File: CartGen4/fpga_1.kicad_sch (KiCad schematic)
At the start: 5 parts, among them U9 LFXP2-8E-5MN132C

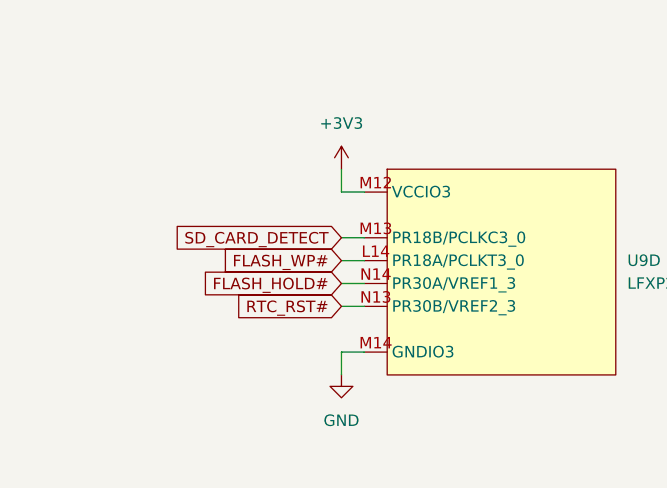
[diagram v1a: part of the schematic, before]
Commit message: Wired general purpose signals
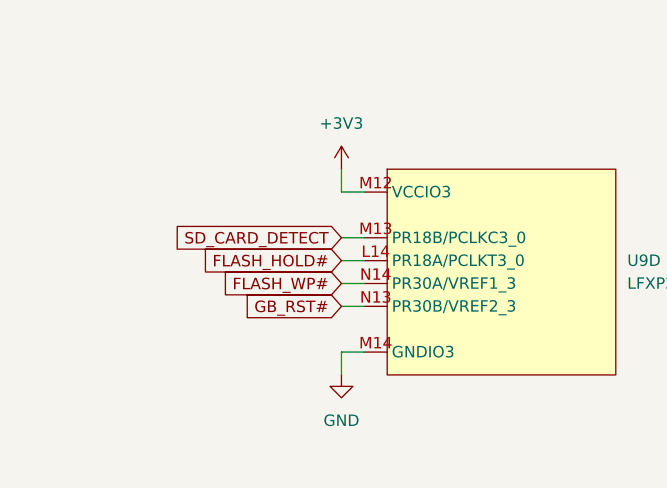
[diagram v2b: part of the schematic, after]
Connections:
- net FLASH_HOLD#: now also U9.L14 (PR18A/PCLKT3_0); no longer U9.N14 (PR30A/VREF1_3)
- net FLASH_WP#: now also U9.N14 (PR30A/VREF1_3); no longer U9.L14 (PR18A/PCLKT3_0)
- net RTC_RST# renamed GB_RST#
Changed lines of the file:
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@@
     )
   )
-  (global_label "FLASH_WP#" (shape input) (at 50.8 151.13 180) (fields_autoplaced)
+  (global_label "FLASH_HOLD#" (shape input) (at 50.8 151.13 180) (fields_autoplaced)
     (effects (font (size 1.27 1.27)) (justify right))
-    (property "Intersheet References" "${INTERSHEET_REFS}" (id 0) (at 37.6826 151.0506 0)
+    (property "Intersheet References" "${INTERSHEET_REFS}" (id 0) (at 35.445 151.0506 0)
       (effects (font (size 1.27 1.27)) (justify right) hide)
     )
@@
     )
   )
+  (global_label "GB_RST#" (shape input) (at 50.8 156.21 180) (fields_autoplaced)
+    (effects (font (size 1.27 1.27)) (justify right))
+    (property "Intersheet References" "${INTERSHEET_REFS}" (id 0) (at 40.1621 156.2894 0)
+      (effects (font (size 1.27 1.27)) (justify right) hide)
+    )
+  )
   (global_label "GB_ADDR[0..15]" (shape input) (at 115.57 39.37 180) (fields_autoplaced)
     (effects (font (size 1.27 1.27)) (justify right))
@@
     )
   )
-  (global_label "RTC_RST#" (shape input) (at 50.8 156.21 180) (fields_autoplaced)
+  (global_label "FLASH_WP#" (shape input) (at 50.8 153.67 180) (fields_autoplaced)
     (effects (font (size 1.27 1.27)) (justify right))
-    (property "Intersheet References" "${INTERSHEET_REFS}" (id 0) (at 39.1945 156.1306 0)
+    (property "Intersheet References" "${INTERSHEET_REFS}" (id 0) (at 37.6826 153.5906 0)
       (effects (font (size 1.27 1.27)) (justify right) hide)
     )
@@
       (effects (font (size 1.27 1.27)) (justify right) hide)
     )
-  )
-  (global_label "FLASH_HOLD#" (shape input) (at 50.8 153.67 180) (fields_autoplaced)
-    (effects (font (size 1.27 1.27)) (justify right))
-    (property "Intersheet References" "${INTERSHEET_REFS}" (id 0) (at 35.445 153.5906 0)
-      (effects (font (size 1.27 1.27)) (justify right) hide)
-    )

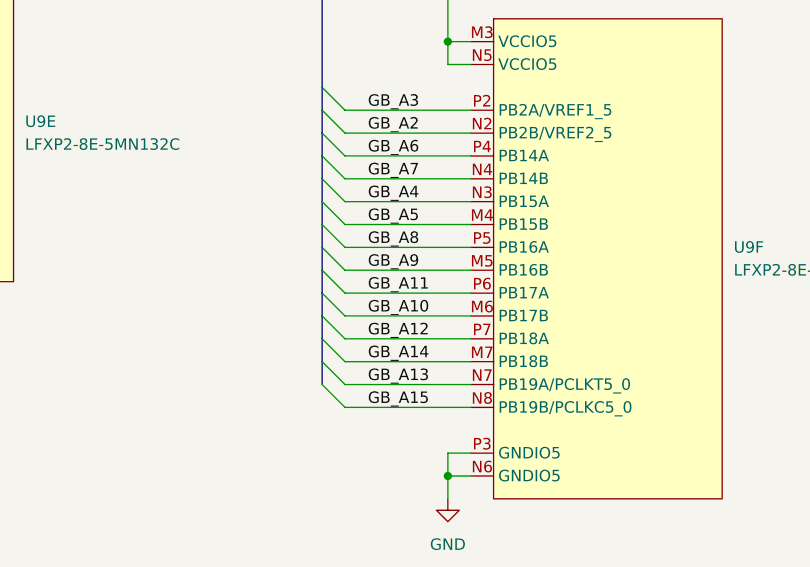
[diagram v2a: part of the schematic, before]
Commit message: Wired 1V2 and 1V8 around FPGA and RAM
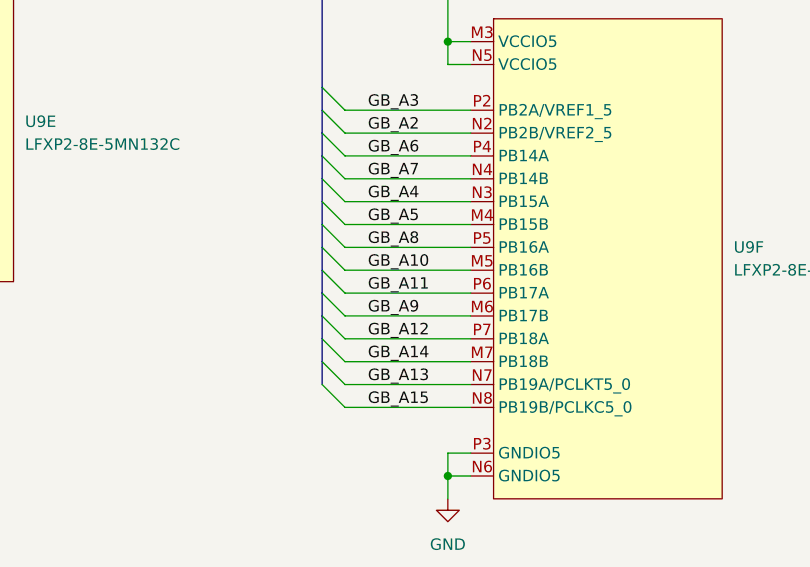
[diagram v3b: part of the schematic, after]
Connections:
- net GB_A10: now also U9.M5 (PB16B); no longer U9.M6 (PB17B)
- net GB_A9: now also U9.M6 (PB17B); no longer U9.M5 (PB16B)
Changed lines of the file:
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@@
     (effects (font (size 1.27 1.27)) (justify left bottom))
   )
-  (label "GB_A9" (at 130.81 85.09 0)
+  (label "GB_A9" (at 130.81 90.17 0)
     (effects (font (size 1.27 1.27)) (justify left bottom))
   )
@@
     (effects (font (size 1.27 1.27)) (justify left bottom))
   )
-  (label "GB_A10" (at 130.81 90.17 0)
-    (effects (font (size 1.27 1.27)) (justify left bottom))
-  )
   (label "GB_A4" (at 130.81 77.47 0)
     (effects (font (size 1.27 1.27)) (justify left bottom))
@@
     (effects (font (size 1.27 1.27)) (justify left bottom))
   )
+  (label "GB_A10" (at 130.81 85.09 0)
+    (effects (font (size 1.27 1.27)) (justify left bottom))
+  )

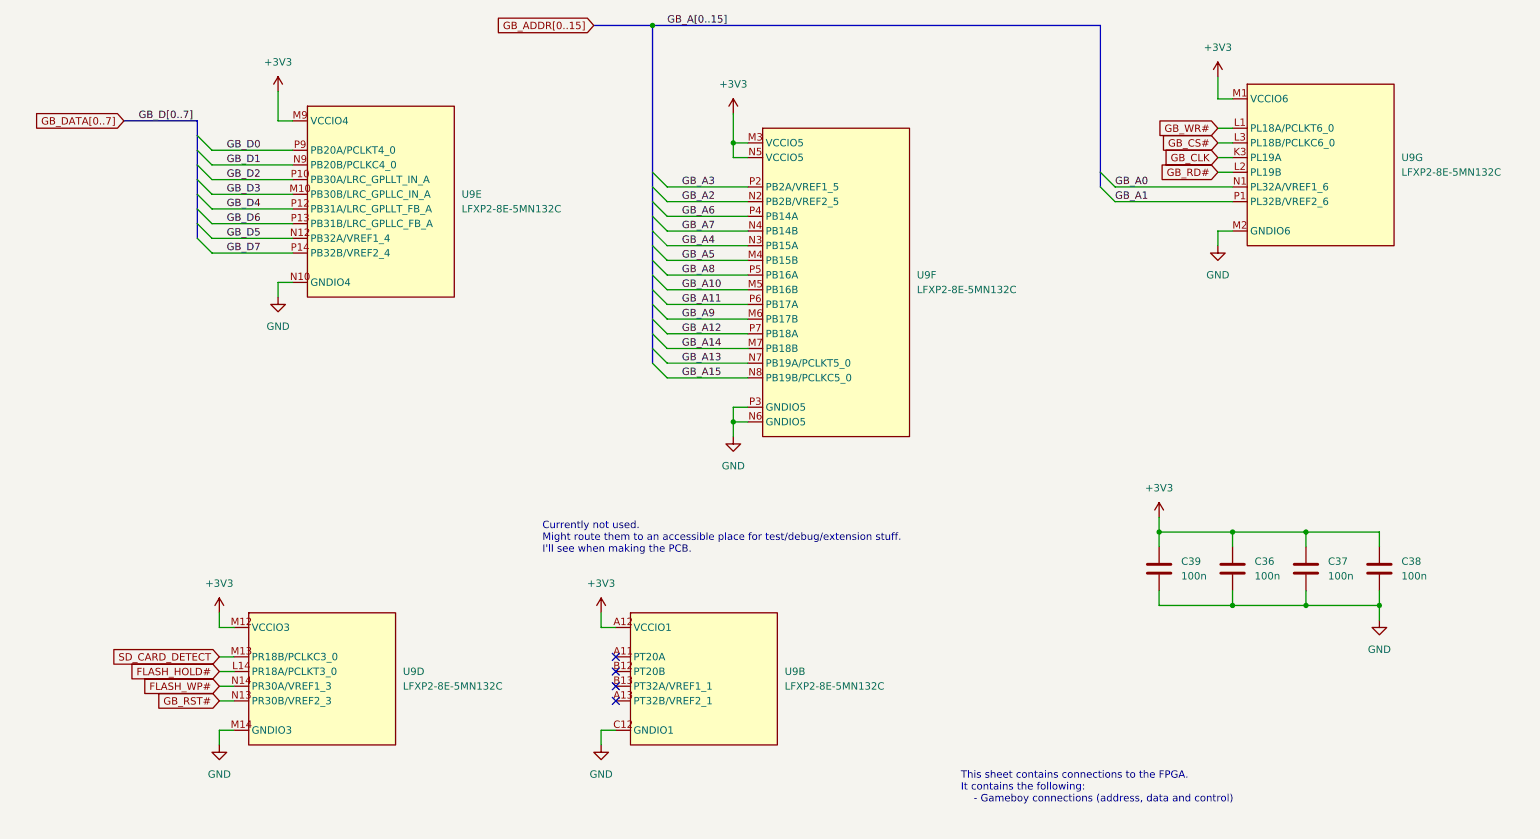
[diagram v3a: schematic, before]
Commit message: Rerouted some RAM and GB CTRL traces
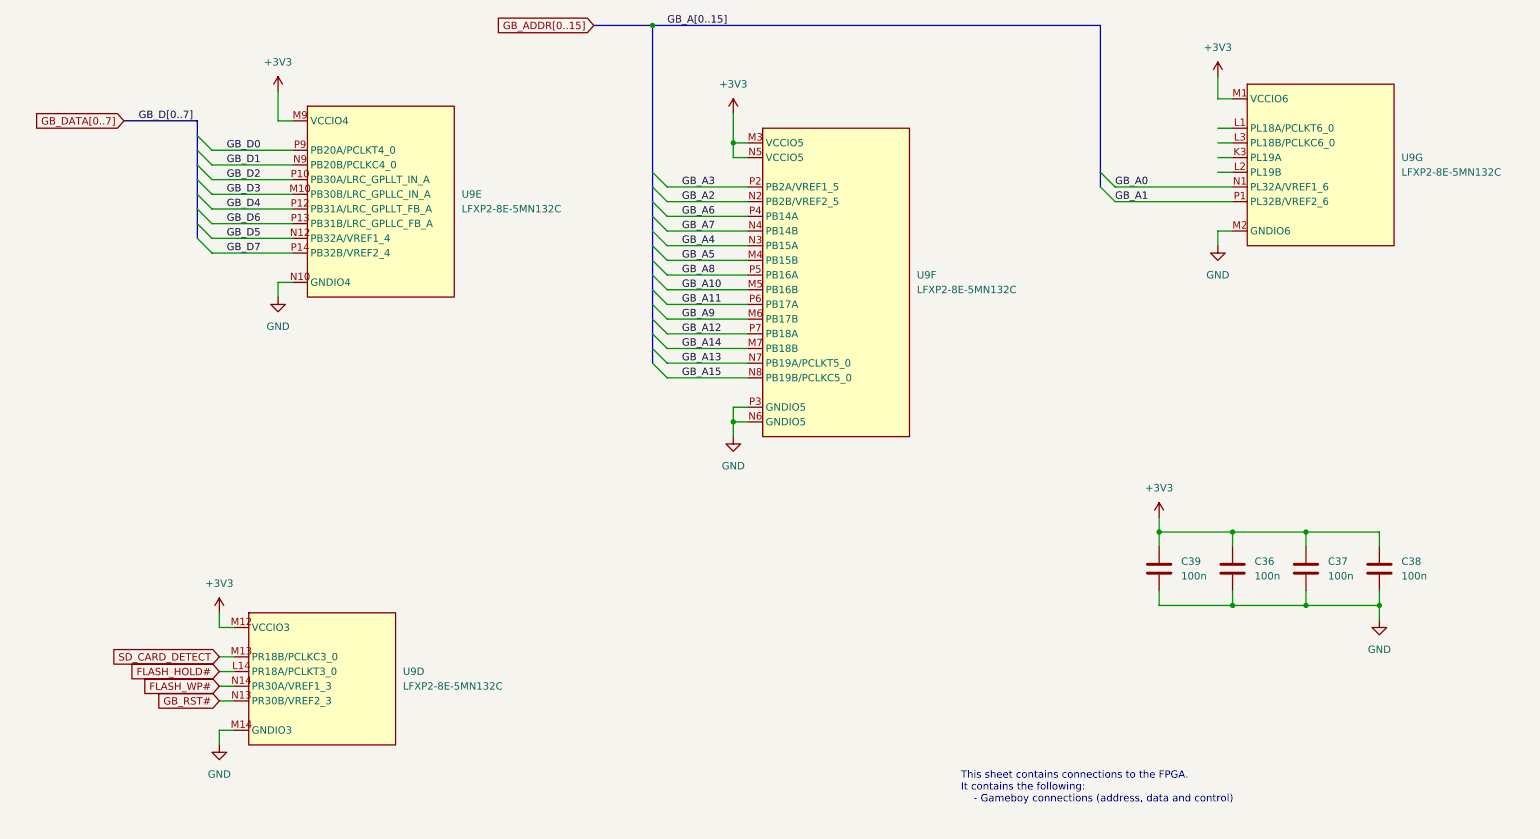
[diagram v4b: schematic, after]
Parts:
- removed unit 2 of U9
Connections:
- net GB_CLK: no longer names the net of U9.K3 (PL19A)
- net GB_CS#: no longer names the net of U9.L3 (PL18B/PCLKC6_0)
- net GB_RD#: no longer names the net of U9.L2 (PL19B)
- net GB_WR#: no longer names the net of U9.L1 (PL18A/PCLKT6_0)
- no-connect marks 4 -> 0
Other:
- note removed: "Currently not used. Might route them to an accessible place for test/debug/extension stuff. I'll see when making the PCB."
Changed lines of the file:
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@@
   (junction (at 139.7 59.69) (diameter 0) (color 0 0 0 0)
   )
-  (no_connect (at 119.38 156.21))
-  (no_connect (at 119.38 153.67))
-  (no_connect (at 119.38 151.13))
-  (no_connect (at 119.38 148.59))
   (bus_entry (at 46.99 73.66) (size 2.54 2.54)
     (stroke (width 0) (type default) (color 0 0 0 0))
@@
     (stroke (width 0) (type default) (color 0 0 0 0))
   )
-  (wire (pts (xy 116.84 143.51) (xy 116.84 140.97))
-    (stroke (width 0) (type default) (color 0 0 0 0))
-  )
-  (wire (pts (xy 119.38 161.29) (xy 116.84 161.29))
-    (stroke (width 0) (type default) (color 0 0 0 0))
-  )
   (wire (pts (xy 49.53 63.5) (xy 63.5 63.5))
     (stroke (width 0) (type default) (color 0 0 0 0))
@@
     (stroke (width 0) (type default) (color 0 0 0 0))
   )
-  (wire (pts (xy 116.84 161.29) (xy 116.84 163.83))
-    (stroke (width 0) (type default) (color 0 0 0 0))
-  )
   (wire (pts (xy 238.76 139.7) (xy 251.46 139.7))
     (stroke (width 0) (type default) (color 0 0 0 0))
@@
   )
   (wire (pts (xy 142.24 105.41) (xy 139.7 105.41))
-    (stroke (width 0) (type default) (color 0 0 0 0))
-  )
-  (wire (pts (xy 119.38 143.51) (xy 116.84 143.51))
     (stroke (width 0) (type default) (color 0 0 0 0))
   )
@@
     (effects (font (size 1.27 1.27)) (justify left bottom))
   )
-  (text "Currently not used.\nMight route them to an accessible place for test/debug/extension stuff.\nI'll see when making the PCB."
-    (at 106.68 130.81 0)
-    (effects (font (size 1.27 1.27)) (justify left bottom))
-  )
   (label "GB_D5" (at 52.07 76.2 0)
     (effects (font (size 1.27 1.27)) (justify left bottom))
@@
   (label "GB_A5" (at 130.81 80.01 0)
     (effects (font (size 1.27 1.27)) (justify left bottom))
-  )
-  (global_label "GB_CS#" (shape input) (at 223.52 59.69 180) (fields_autoplaced)
-    (effects (font (size 1.27 1.27)) (justify right))
-    (property "Intersheet References" "${INTERSHEET_REFS}" (id 0) (at 213.8498 59.6106 0)
-      (effects (font (size 1.27 1.27)) (justify right) hide)
-    )
   )
   (global_label "FLASH_HOLD#" (shape input) (at 50.8 151.13 180) (fields_autoplaced)
@@
     )
   )
-  (global_label "GB_RD#" (shape input) (at 223.52 64.77 180) (fields_autoplaced)
-    (effects (font (size 1.27 1.27)) (justify right))
-    (property "Intersheet References" "${INTERSHEET_REFS}" (id 0) (at 213.7893 64.6906 0)
-      (effects (font (size 1.27 1.27)) (justify right) hide)
-    )
-  )
   (global_label "SD_CARD_DETECT" (shape input) (at 50.8 148.59 180) (fields_autoplaced)
     (effects (font (size 1.27 1.27)) (justify right))
     (property "Intersheet References" "${INTERSHEET_REFS}" (id 0) (at 32.3002 148.6694 0)
-      (effects (font (size 1.27 1.27)) (justify right) hide)
-    )
-  )
-  (global_label "GB_CLK" (shape input) (at 223.52 62.23 180) (fields_autoplaced)
-    (effects (font (size 1.27 1.27)) (justify right))
-    (property "Intersheet References" "${INTERSHEET_REFS}" (id 0) (at 214.0312 62.1506 0)
-      (effects (font (size 1.27 1.27)) (justify right) hide)
-    )
-  )
-  (global_label "GB_WR#" (shape input) (at 223.52 57.15 180) (fields_autoplaced)
-    (effects (font (size 1.27 1.27)) (justify right))
-    (property "Intersheet References" "${INTERSHEET_REFS}" (id 0) (at 213.6079 57.0706 0)
       (effects (font (size 1.27 1.27)) (justify right) hide)
     )
@@
     (pin "1")
   )
-  (symbol (lib_id "power:+3V3") (at 116.84 140.97 0) (unit 1)
-    (in_bom yes) (on_board yes) (fields_autoplaced)
-    (property "Reference" "#PWR090" (id 0) (at 116.84 144.78 0)
-      (effects (font (size 1.27 1.27)) hide)
-    )
-    (property "Value" "+3V3" (id 1) (at 116.84 135.89 0))
-    (property "Footprint" "" (id 2) (at 116.84 140.97 0)
-      (effects (font (size 1.27 1.27)) hide)
-    )
-    (property "Datasheet" "" (id 3) (at 116.84 140.97 0)
-      (effects (font (size 1.27 1.27)) hide)
-    )
-    (pin "1")
-  )
   (symbol (lib_id "power:+3V3") (at 50.8 140.97 0) (unit 1)
     (in_bom yes) (on_board yes) (fields_autoplaced)
@@
     (pin "1")
   )
-  (symbol (lib_id "FPGA_Lattice:LFXP2-8E-5MN132C") (at 121.92 140.97 0) (unit 2)
-    (in_bom yes) (on_board yes) (fields_autoplaced)
-    (property "Reference" "U9" (id 0) (at 148.59 151.1299 0)
-      (effects (font (size 1.27 1.27)) (justify left))
-    )
-    (property "Value" "LFXP2-8E-5MN132C" (id 1) (at 148.59 153.6699 0)
-      (effects (font (size 1.27 1.27)) (justify left))
-    )
-    (property "Footprint" "SamacSys_Parts:BGA132C50P14X14_800X800X135" (id 2) (at 125.73 138.43 0)
-      (effects (font (size 1.27 1.27)) hide)
-    )
-    (property "Datasheet" "https://www.latticesemi.com/view_document?document_id=24635" (id 3) (at 125.73 138.43 0)
-      (effects (font (size 1.27 1.27)) hide)
-    )
-    (property "Critical" "Y" (id 4) (at 121.92 140.97 0)
-      (effects (font (size 1.27 1.27)) hide)
-    )
-    (property "Description" "FPGA - Field Programmable Gate Array 8K LUTs 86I/O Inst- on DSP 1.2V -5 Spd" (id 5) (at 121.92 140.97 0)
-      (effects (font (size 1.27 1.27)) hide)
-    )
-    (property "MFN" "Lattice" (id 6) (at 121.92 140.97 0)
-      (effects (font (size 1.27 1.27)) hide)
-    )
-    (property "MFP" "LFXP2-8E-5MN132C" (id 7) (at 121.92 140.97 0)
-      (effects (font (size 1.27 1.27)) hide)
-    )
-    (property "Notes" "FPGA used for the bulk of the cartridge's functions (MBC emulation, SPI bridge, MMU functions, etc.)." (id 8) (at 121.92 140.97 0)
-      (effects (font (size 1.27 1.27)) hide)
-    )
-    (property "Package ID" "CSBGA-132" (id 9) (at 121.92 140.97 0)
-      (effects (font (size 1.27 1.27)) hide)
-    )
-    (property "Source" "SPEC" (id 10) (at 121.92 140.97 0)
-      (effects (font (size 1.27 1.27)) hide)
-    )
-    (pin "A11")
-    (pin "A12")
-    (pin "A13")
-    (pin "B12")
-    (pin "B13")
-    (pin "C12")
-  )
   (symbol (lib_id "power:GND") (at 139.7 110.49 0) (unit 1)
     (in_bom yes) (on_board yes) (fields_autoplaced)
@@
       (effects (font (size 1.27 1.27)) hide)
     )
-    (pin "1")
-  )
-  (symbol (lib_id "power:GND") (at 116.84 163.83 0) (unit 1)
-    (in_bom yes) (on_board yes) (fields_autoplaced)
-    (property "Reference" "#PWR091" (id 0) (at 116.84 170.18 0)
-      (effects (font (size 1.27 1.27)) hide)
-    )
-    (property "Value" "GND" (id 1) (at 116.84 168.91 0))
-    (property "Footprint" "" (id 2) (at 116.84 163.83 0)
-      (effects (font (size 1.27 1.27)) hide)
-    )
-    (property "Datasheet" "" (id 3) (at 116.84 163.83 0)
-      (effects (font (size 1.27 1.27)) hide)
-    )

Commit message: Added external test header to schematic
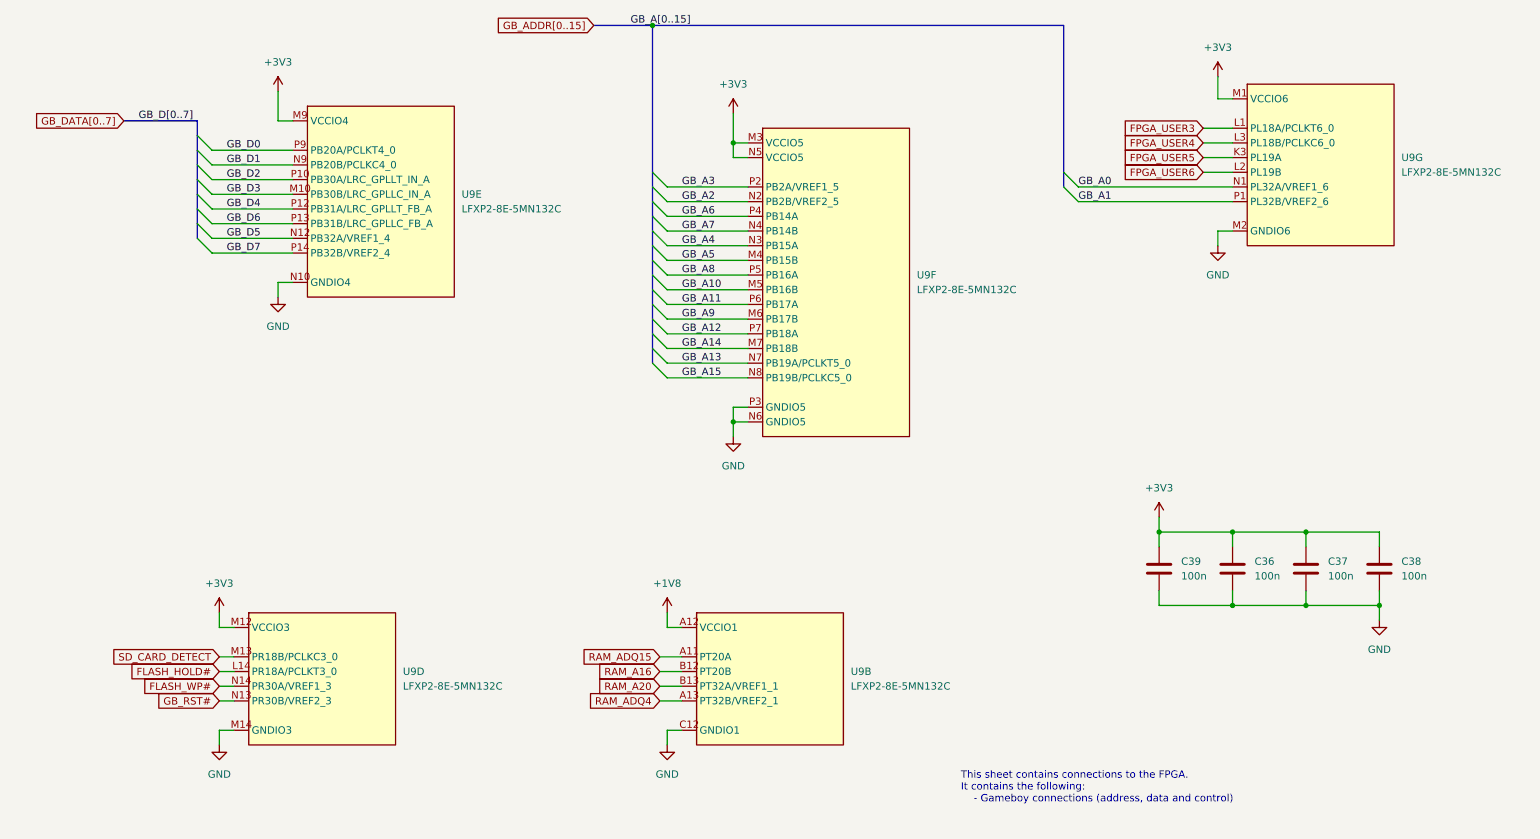
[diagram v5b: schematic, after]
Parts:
- added unit 2 of U9
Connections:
- net GND: now also U9.C12 (GNDIO1)
- net FPGA_USER5: now reaches U9.K3 (PL19A)
- net FPGA_USER3: now reaches U9.L1 (PL18A/PCLKT6_0)
- net FPGA_USER6: now reaches U9.L2 (PL19B)
- net FPGA_USER4: now reaches U9.L3 (PL18B/PCLKC6_0)
- new net +1V8: U9.A12 (VCCIO1)
- new net RAM_A16: U9.B12 (PT20B)
- new net RAM_A20: U9.B13 (PT32A/VREF1_1)
- new net RAM_ADQ15: U9.A11 (PT20A)
- new net RAM_ADQ4: U9.A13 (PT32B/VREF2_1)
